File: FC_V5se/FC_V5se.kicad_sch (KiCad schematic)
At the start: 75 parts, among them IC3 RV-3028-C7_32.768kHz_1ppm_TA_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, J12 USB_C_Receptacle_USB2.0_16P, J16 DEBUG, J18 Payload, J22 SWD Port, J3 Life Makes Lemonade, J5 BM04B-SRSS-TB(LF)(SN), SW1 KMR2, SW2 KMR2, U13 E22-400M30S, U14 TCA4307DGKR, U15 LIS2MDL, U2 ZDSD04GLGEAG, U3 TCA9548APWR, U30 E28-2G4M27S, U7 LSM6DSOTR

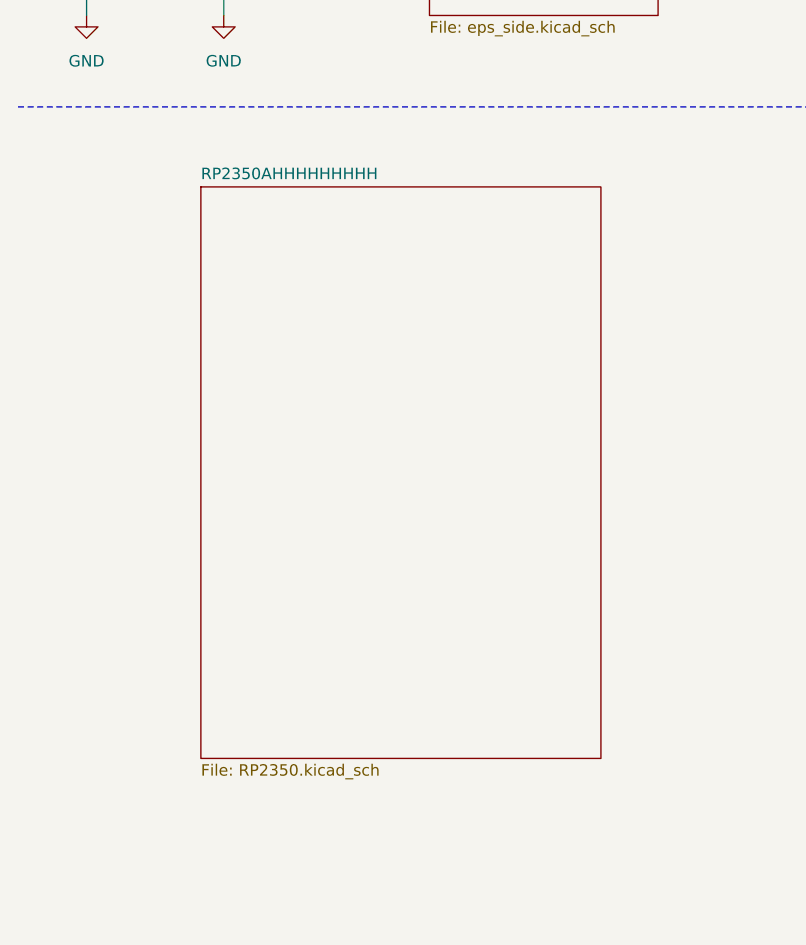
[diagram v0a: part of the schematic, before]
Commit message: V5e: Delete RP2350
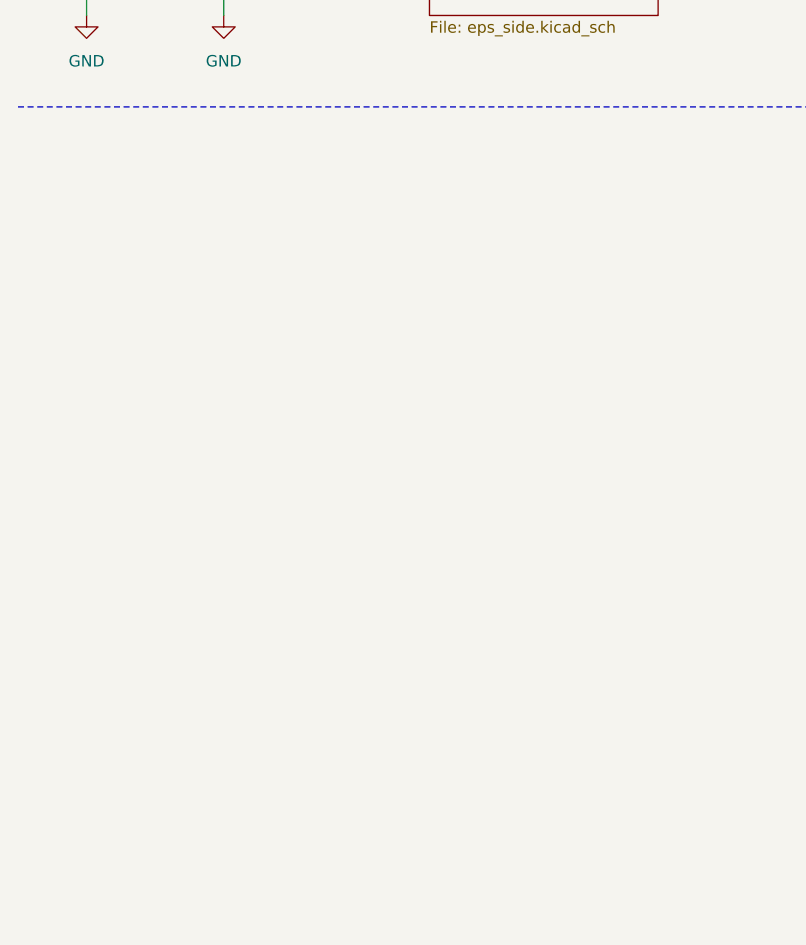
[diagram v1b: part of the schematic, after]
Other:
- removed sheet RP2350AHHHHHHHHH
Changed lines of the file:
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@@
-	)
-	(sheet
-		(at 31.75 86.36)
-		(size 44.45 63.5)
-		(exclude_from_sim no)
-		(in_bom yes)
-		(on_board yes)
-		(dnp no)
-		(fields_autoplaced yes)
-		(stroke
-			(width 0.1524)
-			(type solid)
-		)
-		(fill
-			(color 0 0 0 0)
-		)
-		(property "Sheetname" "RP2350AHHHHHHHHH"
-			(at 31.75 85.6484 0)
-			(show_name no)
-			(do_not_autoplace no)
-			(effects
-				(font
-					(size 1.27 1.27)
-				)
-				(justify left bottom)
-			)
-		)
-		(property "Sheetfile" "RP2350.kicad_sch"
-			(at 31.75 150.4446 0)
-			(show_name no)
-			(do_not_autoplace no)
-			(effects
-				(font
-					(size 1.27 1.27)
-				)
-				(justify left top)
-			)
-		)
-		(instances
-			(project "FC_V5se"
-				(path "/c64c0d72-a9f6-4f3a-891e-1f647558f538"
-					(page "6")
-				)
-			)
-		)
 	)
 	(sheet

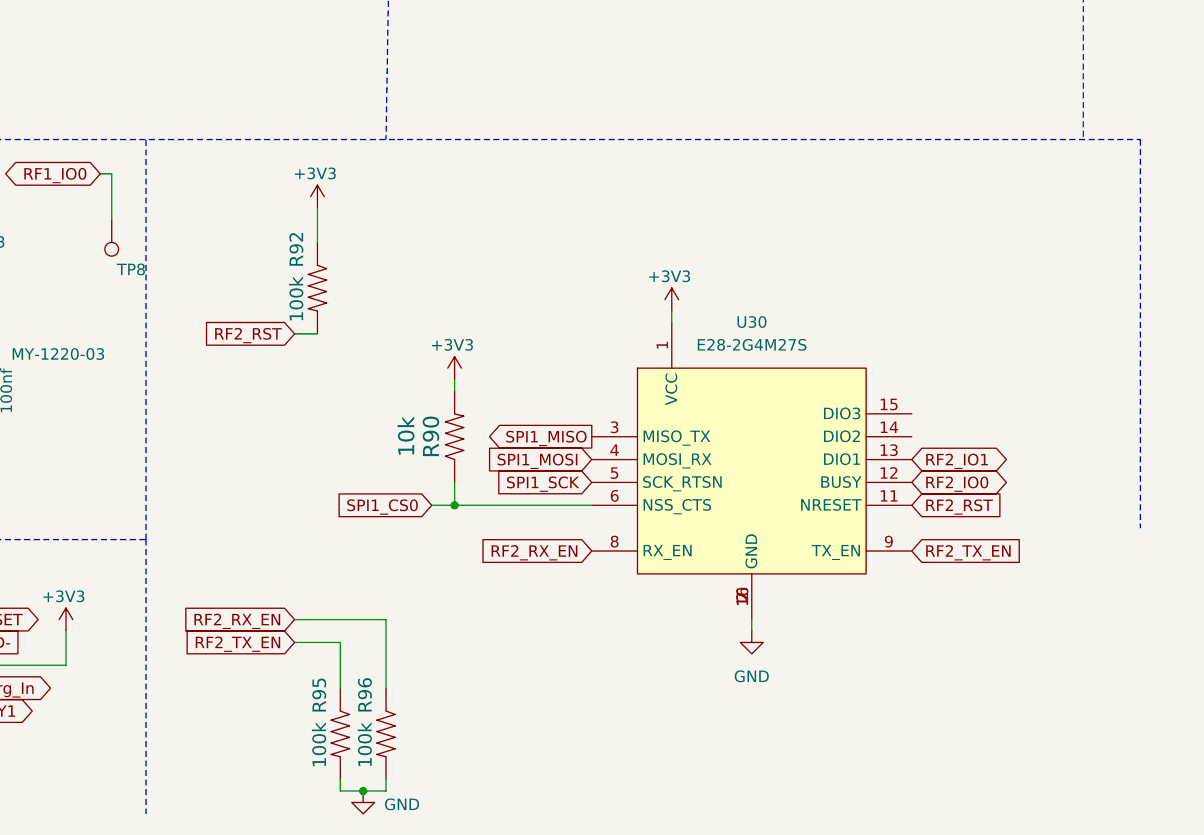
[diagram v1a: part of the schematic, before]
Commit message: V5se: Deleted E28 S-Band Radio
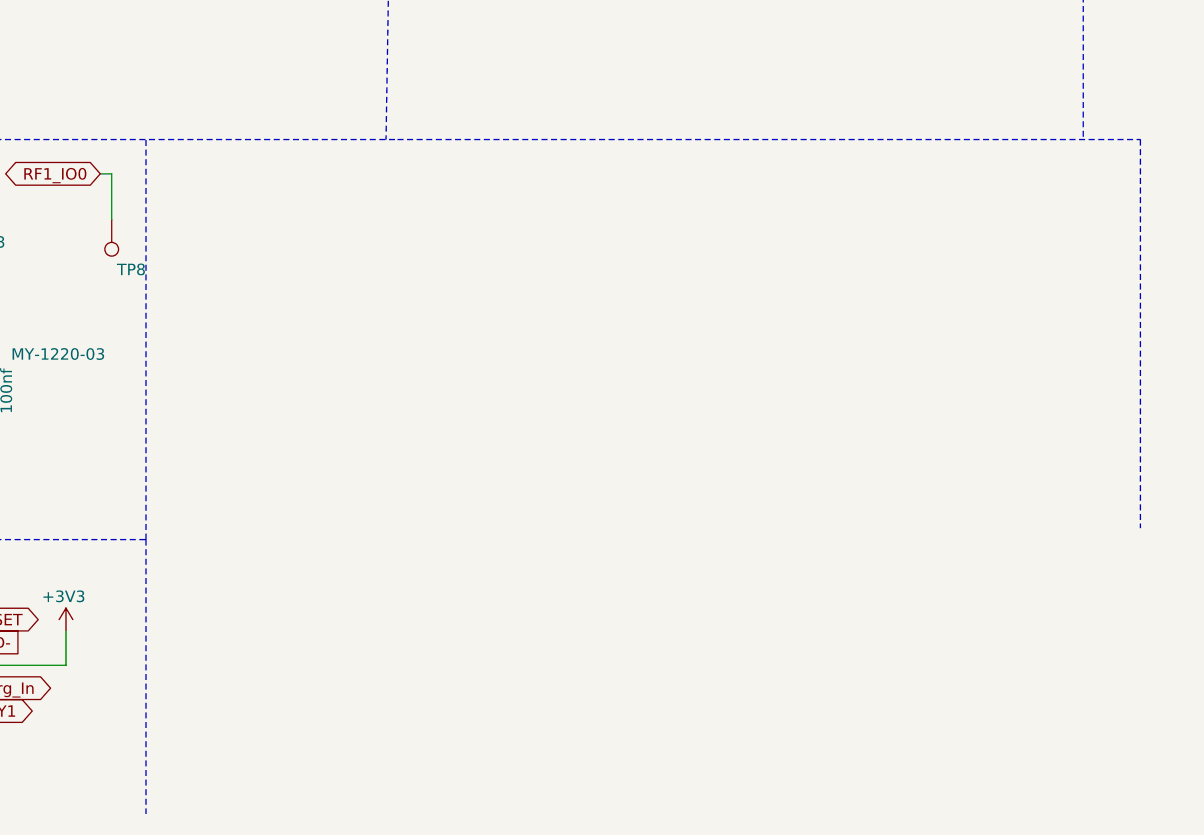
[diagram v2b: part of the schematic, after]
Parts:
- removed R90: 10k, Resistor_SMD:R_0603_1608Metric, symbol mainboard:RESISTOR0603
- removed R92, R95, R96: 100k, Resistor_SMD:R_0603_1608Metric, symbol mainboard:R-US_R0603
- removed U30: E28-2G4M27S, easyeda2kicad:WIRELM-SMD_E28-2G4M2XS, symbol easyeda2kicad:E28-2G4M27S

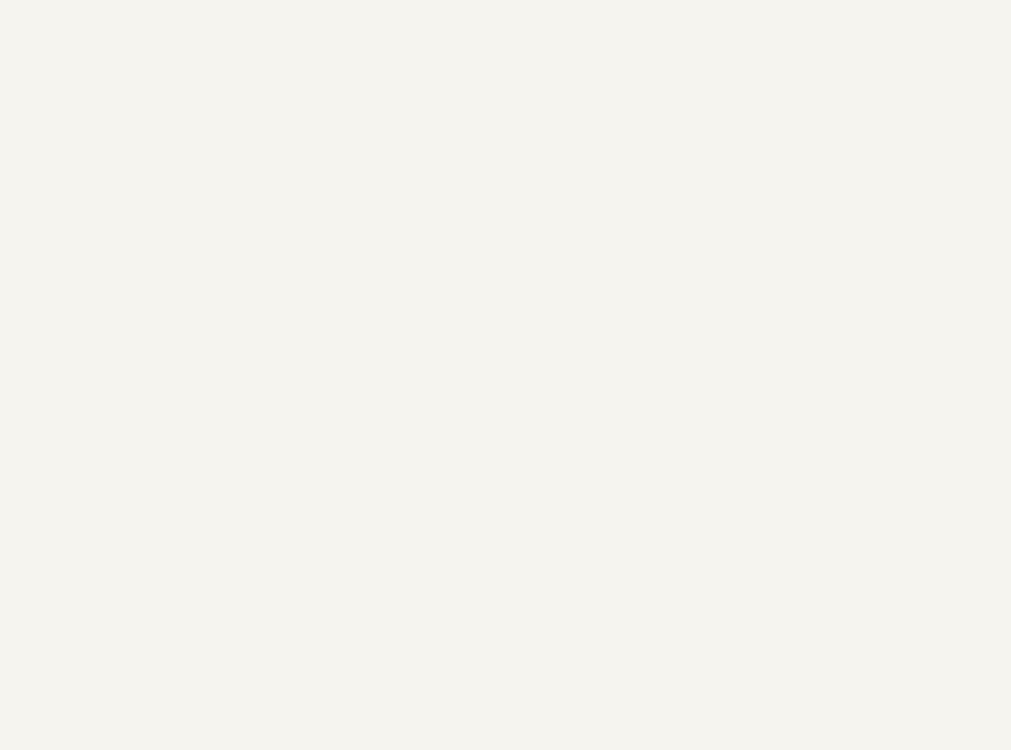
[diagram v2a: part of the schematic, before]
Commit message: V5se: Selected STM32U5A5QJI6Q as uController
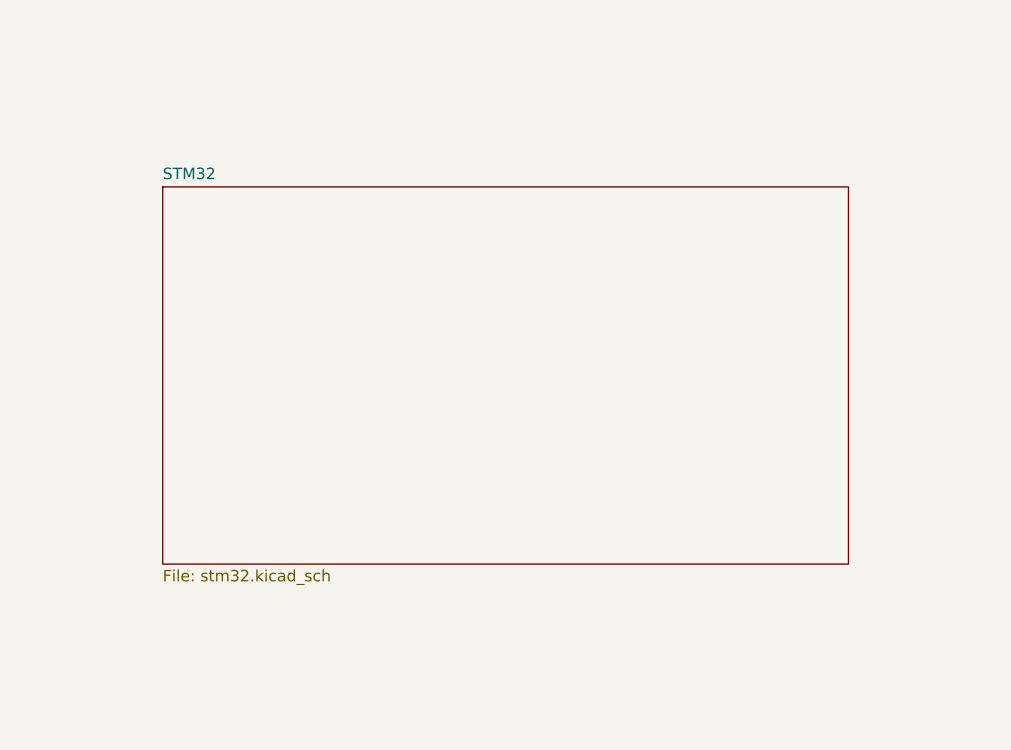
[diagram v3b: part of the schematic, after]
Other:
- added sheet STM32 (stm32.kicad_sch)
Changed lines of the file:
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@@
+		)
+	)
+	(sheet
+		(at 57.15 99.06)
+		(size 76.2 41.91)
+		(exclude_from_sim no)
+		(in_bom yes)
+		(on_board yes)
+		(dnp no)
+		(fields_autoplaced yes)
+		(stroke
+			(width 0.1524)
+			(type solid)
+		)
+		(fill
+			(color 0 0 0 0)
+		)
+		(property "Sheetname" "STM32"
+			(at 57.15 98.3484 0)
+			(show_name no)
+			(do_not_autoplace no)
+			(effects
+				(font
+					(size 1.27 1.27)
+				)
+				(justify left bottom)
+			)
+		)
+		(property "Sheetfile" "stm32.kicad_sch"
+			(at 57.15 141.5546 0)
+			(show_name no)
+			(do_not_autoplace no)
+			(effects
+				(font
+					(size 1.27 1.27)
+				)
+				(justify left top)
+			)
+		)
+		(instances
+			(project "FC_V5se"
+				(path "/c64c0d72-a9f6-4f3a-891e-1f647558f538"
+					(page "2")
+				)
+			)
 		)
 	)

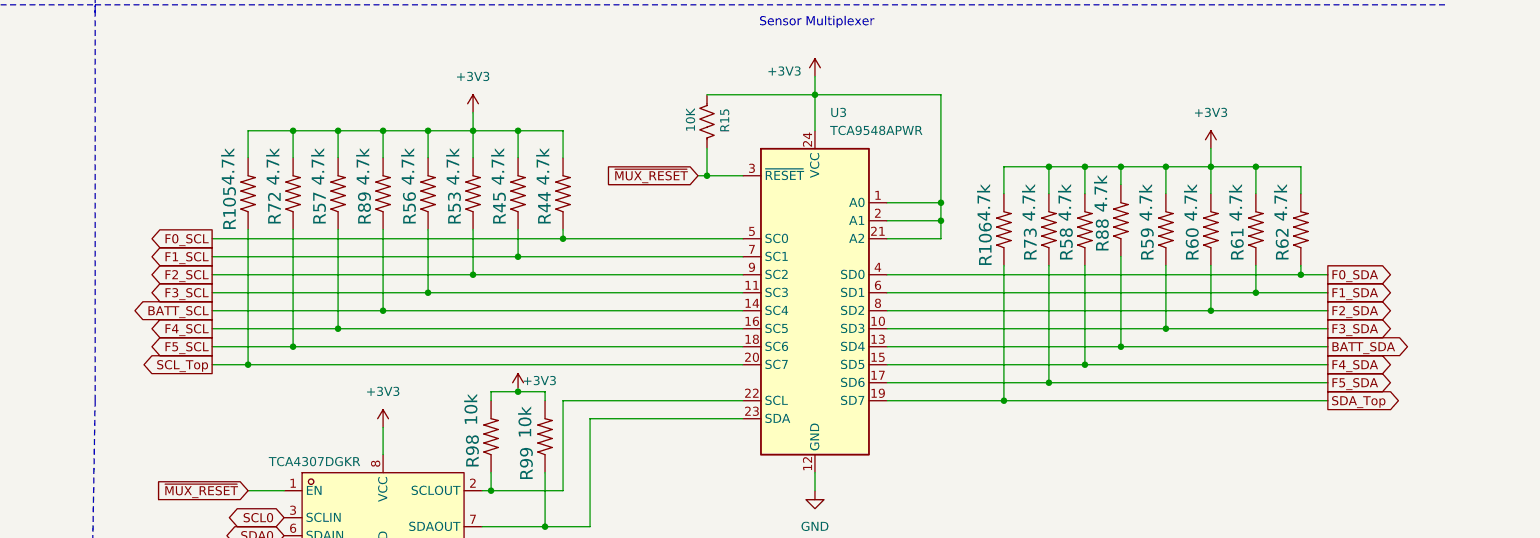
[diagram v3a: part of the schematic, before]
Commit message: V5se: Removed I2C_Top Connections from TCA
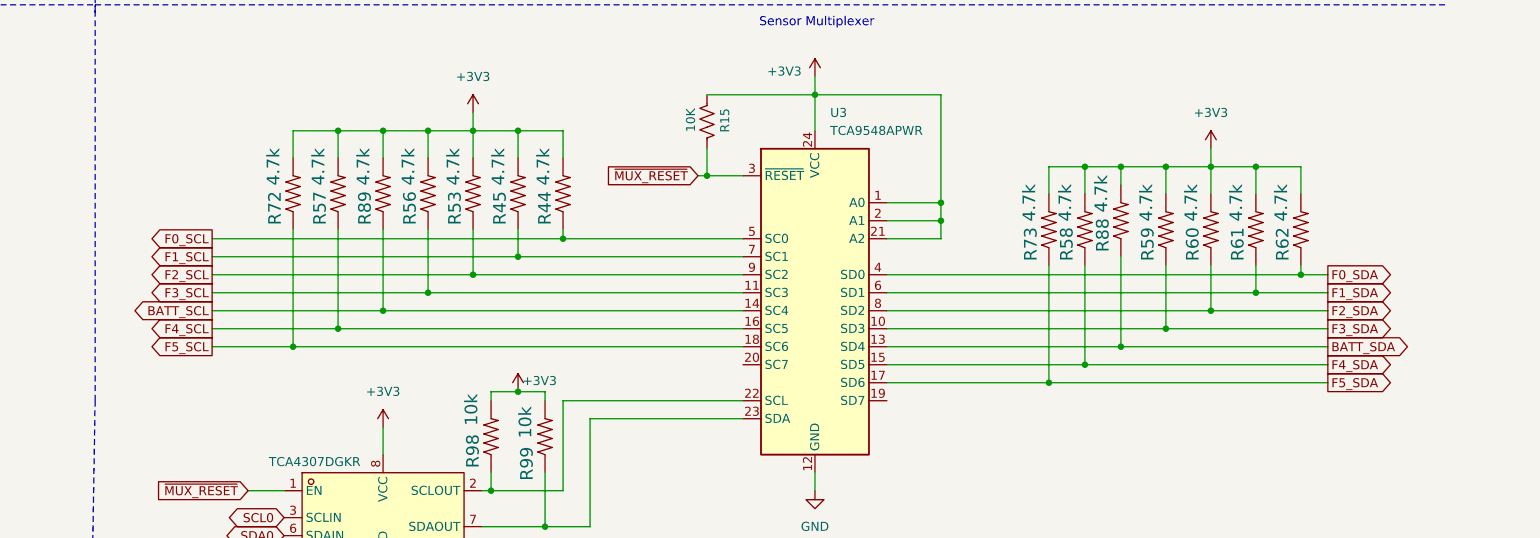
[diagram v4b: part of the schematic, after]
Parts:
- removed R105, R106: 4.7k, Resistor_SMD:R_0603_1608Metric, symbol mainboard:RESISTOR0603
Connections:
- net SCL_Top: no longer U3.20 (SC7)
- net SDA_Top: no longer U3.19 (SD7)

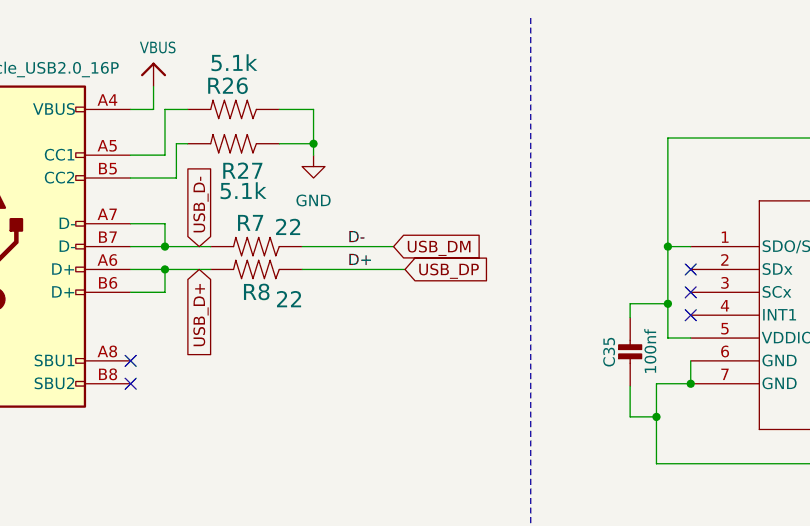
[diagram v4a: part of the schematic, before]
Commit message: V5se: Added Debug Connections to Schematic
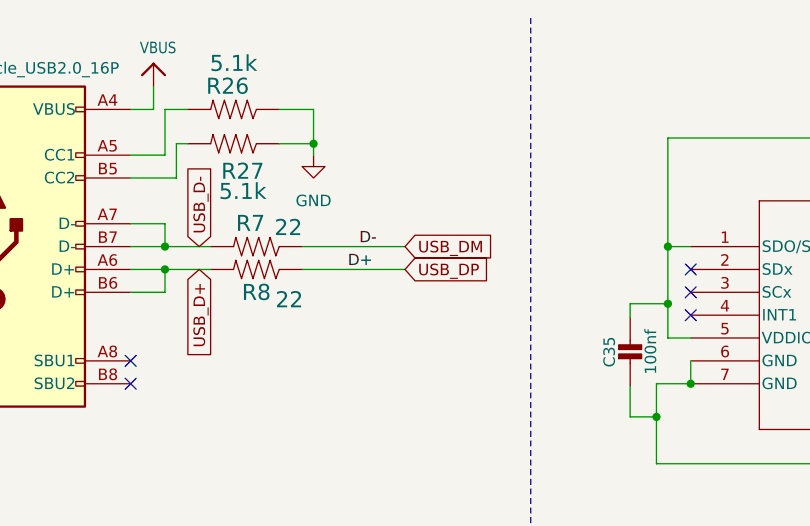
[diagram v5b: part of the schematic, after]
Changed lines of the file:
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@@
 	(wire
 		(pts
-			(xy 191.77 38.1) (xy 201.93 38.1)
+			(xy 191.77 38.1) (xy 203.2 38.1)
 		)
 		(stroke
@@
 	)
 	(label "D-"
-		(at 196.85 38.1 0)
+		(at 198.12 38.1 0)
 		(effects
 			(font
@@
 	(global_label "USB_DM"
 		(shape input)
-		(at 201.93 38.1 0)
+		(at 203.2 38.1 0)
 		(fields_autoplaced yes)
 		(effects
@@
 		)
 		(property "Intersheetrefs" "${INTERSHEET_REFS}"
-			(at 212.4142 38.1 0)
+			(at 213.6842 38.1 0)
 			(hide yes)
 			(show_name no)
